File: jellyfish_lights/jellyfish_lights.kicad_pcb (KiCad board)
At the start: 2 copper layers, 80 x 70.3 mm, 24 parts, among them Q1 AO3400A, SW1 tilt switch, U1 SN74LVC1G14DBV

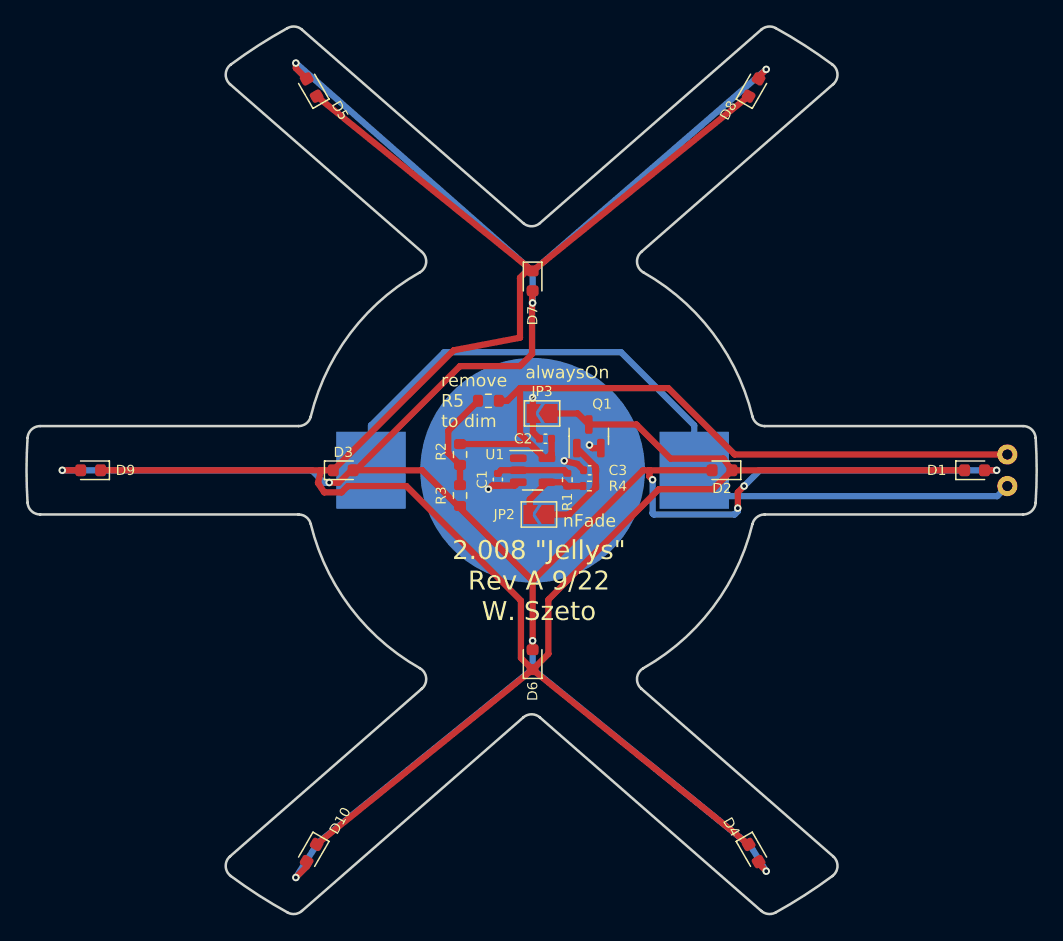
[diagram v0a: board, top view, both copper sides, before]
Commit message: created B01
B01 has a new circuit to do blinking. The op-amp allows for fading of the lights
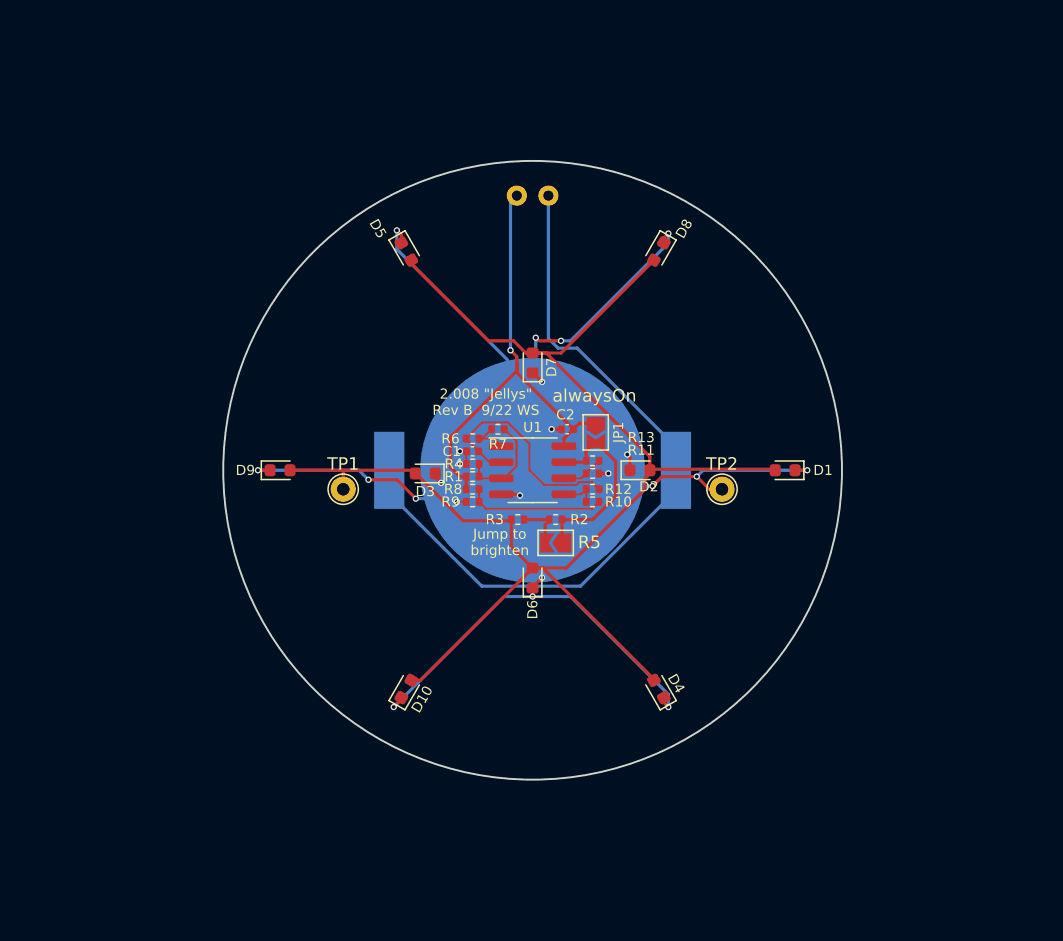
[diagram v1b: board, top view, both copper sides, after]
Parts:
- removed C3: 1uF, Capacitor_SMD:C_0402_1005Metric
- removed JP2: nFade, Jumper:SolderJumper-2_P1.3mm_Open_TrianglePad1.0x1.5mm
- removed JP3: alwaysOn, Jumper:SolderJumper-2_P1.3mm_Open_TrianglePad1.0x1.5mm
- removed Q1: AO3400A, Package_TO_SOT_SMD:SOT-23
- added JP1: alwaysOn, Jumper:SolderJumper-2_P1.3mm_Open_TrianglePad1.0x1.5mm, F.Cu at (180.0, 102.0)
- added R10: 100K, Resistor_SMD:R_0402_1005Metric, F.Cu at (179.8, 107.5)
- added R11: 100K, Resistor_SMD:R_0402_1005Metric, F.Cu at (179.8, 105.2)
- added R12: 100K, Resistor_SMD:R_0402_1005Metric, F.Cu at (179.8, 106.5)
- added R13: 100K, Resistor_SMD:R_0402_1005Metric, F.Cu at (179.8, 104.2)
- added R6: 100K, Resistor_SMD:R_0402_1005Metric, F.Cu at (170.2, 102.5)
- added R7: 100K, Resistor_SMD:R_0402_1005Metric, F.Cu at (172.2, 101.8)
- added R8: 10k, Resistor_SMD:R_0402_1005Metric, F.Cu at (170.2, 106.5)
- added R9: 10k, Resistor_SMD:R_0402_1005Metric, F.Cu at (170.2, 107.5)
- added TP1: LED+, TestPoint:TestPoint_THTPad_D2.0mm_Drill1.0mm, F.Cu at (160.0, 106.5)
- added TP2: LED-, TestPoint:TestPoint_THTPad_D2.0mm_Drill1.0mm, F.Cu at (190.0, 106.5)
- BT1: footprint Battery:BatteryHolder_Keystone_3002_1x2032 -> Battery:BatteryHolder_MPD_BC2003_1x2032
- C1: value 1uF -> 10uF
- R1: value 1M -> 100K
- R2, R3: footprint Resistor_SMD:R_0603_1608Metric -> Resistor_SMD:R_0402_1005Metric
- R5: footprint Resistor_SMD:R_0603_1608Metric -> Jumper:SolderJumper-2_P1.3mm_Open_TrianglePad1.0x1.5mm
- U1: value SN74LVC1G14DBV -> MCP6002-xSN; footprint Package_TO_SOT_SMD:SOT-23-5 -> Package_SO:SOIC-8_3.9x4.9mm_P1.27mm
- moved SW1 43.9 mm to (173.8, 83.2), turned to 0 degrees
- moved D5 15.0 mm to (165.0, 87.7), turned to -60 degrees
- moved D8 15.0 mm to (185.0, 87.7), turned to -120 degrees
- moved D1 15.0 mm to (195.0, 105.0), turned to 180 degrees
- moved D9 15.0 mm to (155.0, 105.0), turned to 0 degrees
- moved D10 15.0 mm to (165.0, 122.3), turned to 60 degrees
- moved D4 15.0 mm to (185.0, 122.3), turned to 120 degrees
- moved R5 12.4 mm to (176.8, 110.8)
- moved R4 9.41 mm to (170.2, 104.5)
- moved R2 9.16 mm to (176.8, 108.9), turned to 180 degrees
- moved R1 7.50 mm to (170.2, 105.5), turned to 180 degrees
- moved D3 6.50 mm to (166.5, 105.2), turned to 180 degrees
- moved D2 6.50 mm to (183.5, 105.0), turned to 0 degrees
- moved D7 6.50 mm to (175.0, 96.5), turned to 90 degrees
- moved D6 6.46 mm to (175.0, 113.5)
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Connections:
- C1 pad 1: Net-(C1-Pad1) -> /triangle
- D1 pad 1: Net-(D1-Pad1) -> GND
- D10 pad 1: Net-(D1-Pad1) -> GND
- D2 pad 1: Net-(D1-Pad1) -> GND
- D3 pad 1: Net-(D1-Pad1) -> GND
- D4 pad 1: Net-(D1-Pad1) -> GND
- D5 pad 1: Net-(D1-Pad1) -> GND
- D6 pad 1: Net-(D1-Pad1) -> GND
- D7 pad 1: Net-(D1-Pad1) -> GND
- D8 pad 1: Net-(D1-Pad1) -> GND
- D9 pad 1: Net-(D1-Pad1) -> GND
- R1 pad 1: Net-(C1-Pad1) -> Net-(R1-Pad1)
- R1 pad 2: Net-(JP2-Pad2) -> VCC
- R2 pad 1: VCC -> /LED_VOLTAGE
- R4 pad 1: Net-(JP2-Pad2) -> GND
- R4 pad 2: Net-(C3-Pad1) -> Net-(R1-Pad1)
- R5 pad 1: VCC -> /LED_VOLTAGE
- U1 pad 1: unconnected-(U1-Pad1) -> Net-(R6-Pad2)
- U1 pad 2: Net-(C1-Pad1) -> /triangle
- U1 pad 3: GND -> Net-(R1-Pad1)
- U1 pad 4: Net-(JP2-Pad2) -> GND
- U1 pad 5: VCC -> Net-(R10-Pad2)
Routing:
- net Net-(D1-Pad1): track 218.1 -> 0.00 mm
- net GND: track 8.83 -> 143.8 mm, vias 4 -> 23
- net Net-(D1-Pad2): track 232.7 -> 114.6 mm, vias 12 -> 0
- net VCC: track 57.4 -> 37.9 mm, vias 0 -> 1
- net /triangle: track 0.00 -> 18.2 mm
- net /LED_VOLTAGE: track 0.00 -> 15.6 mm
- net Net-(R10-Pad1): track 0.00 -> 11.0 mm
- net Net-(C3-Pad1): track 8.42 -> 0.00 mm
- net Net-(R1-Pad1): track 0.00 -> 7.74 mm
- net Net-(JP2-Pad2): track 6.10 -> 0.00 mm
- net Net-(C1-Pad1): track 5.70 -> 0.00 mm
- net Net-(BT1-Pad1): track 63.5 -> 59.2 mm
- net Net-(R2-Pad2): track 8.04 -> 4.11 mm
- net Net-(R11-Pad2): track 0.00 -> 3.36 mm
- net Net-(R6-Pad2): track 0.00 -> 3.30 mm
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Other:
- board size 80 x 70.3 mm -> 49 x 49 mm
- board text added: "2.008 {dblquote}Jellys{dblquote} Rev B 9/22 WS"
- board text added: "Jump to brighten"
- board text added: "LED+"
- board text added: "LED-"
- board text removed: "2.008 {dblquote}Jellys{dblquote} Rev A 9/22 W. Szeto"
- board text removed: "nFade"
- board text removed: "remove R5 to dim"
